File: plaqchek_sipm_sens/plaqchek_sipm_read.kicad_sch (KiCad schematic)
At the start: 32 parts, among them U2 OPA863A, U3 OPA863A, U4 OPA863A, U5 MCP1501T-50E, U9 MCP33131-10-E/MS

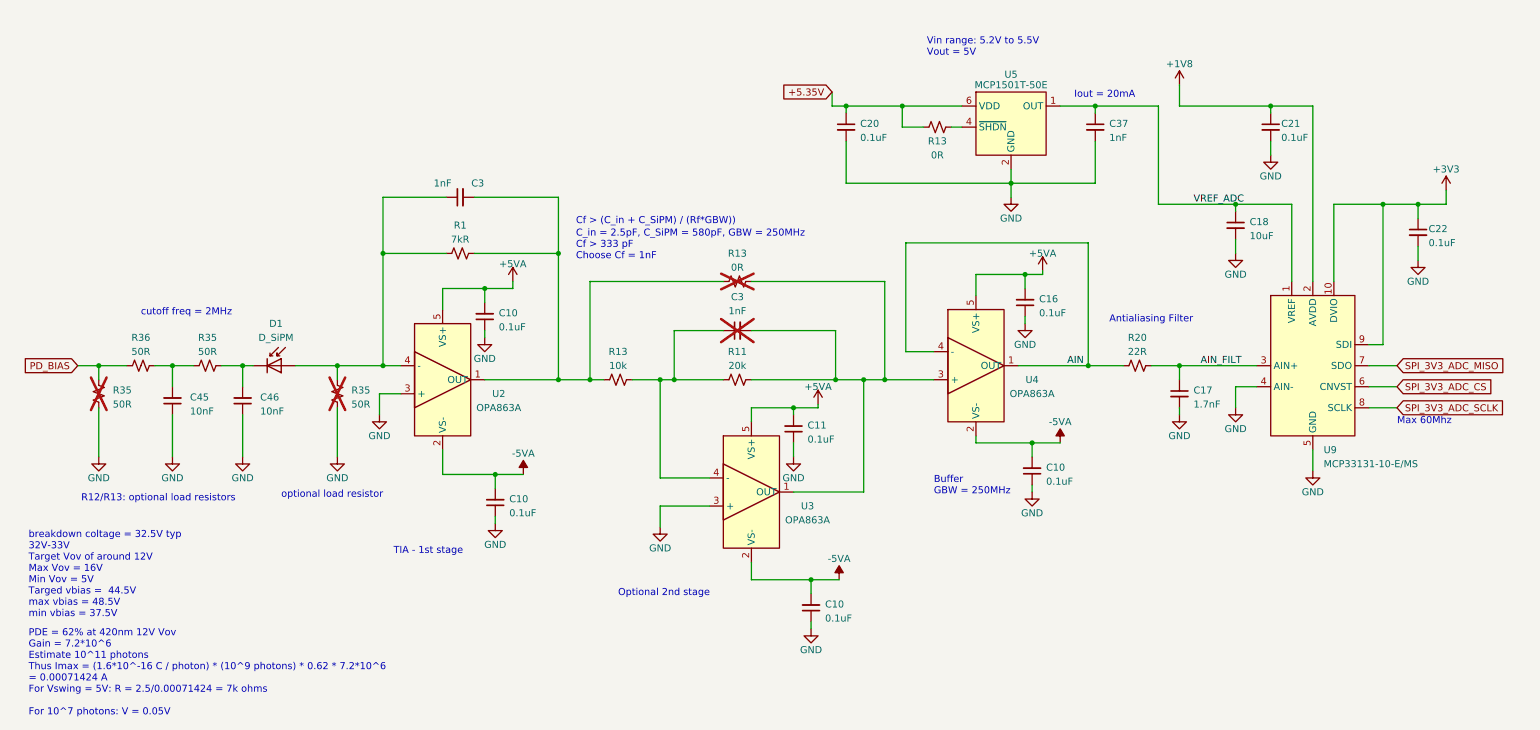
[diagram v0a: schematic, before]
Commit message: modify TIA feedback cap value for new op amp, assign some footprints
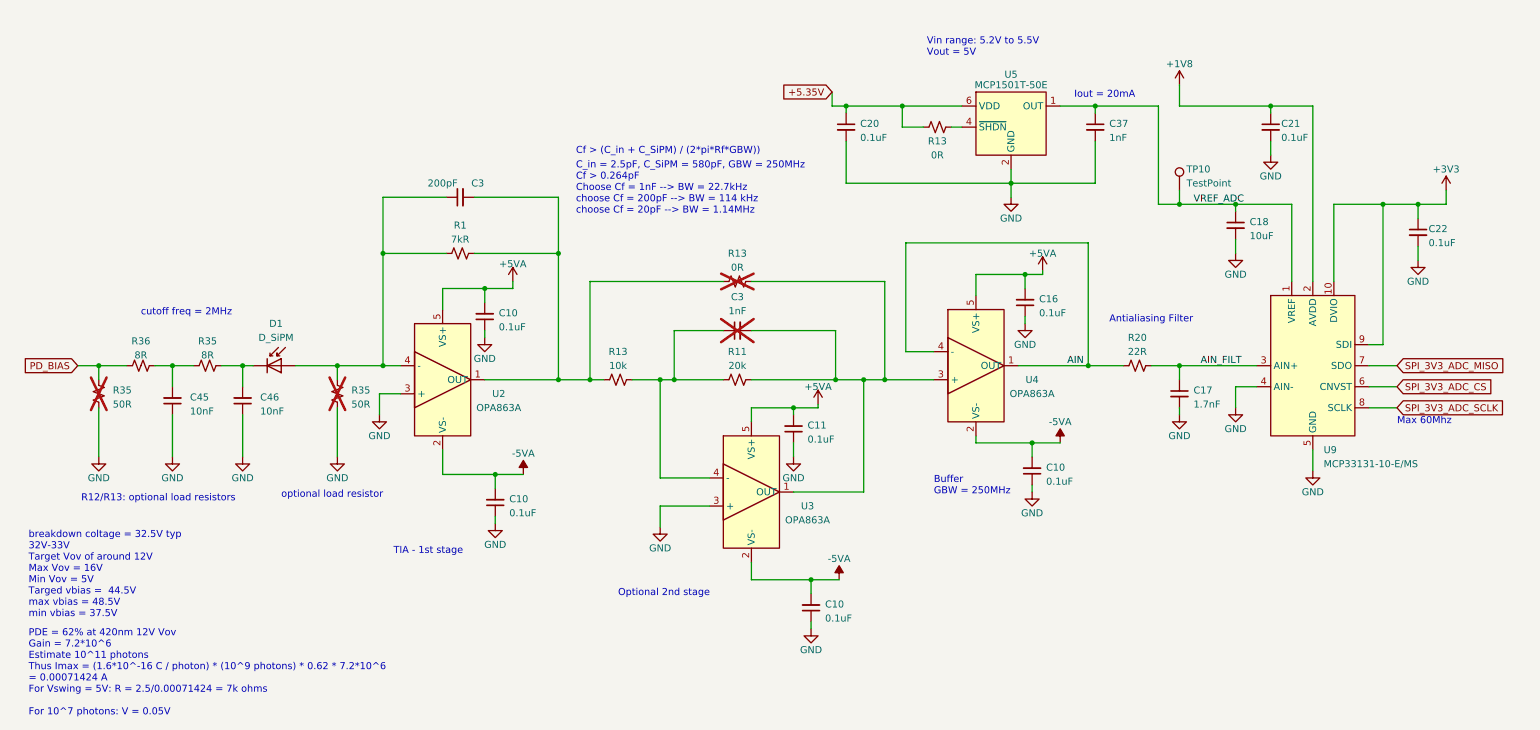
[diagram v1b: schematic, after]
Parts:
- added TP10: TestPoint, TestPoint:TestPoint_Pad_1.5x1.5mm, symbol Connector:TestPoint
- C10, C11, C16, C17, C18, C20, C21, C22, C3, C37, C45, C46: footprint (none) -> Capacitor_SMD:C_0603_1608Metric_Pad1.08x0.95mm_HandSolder
- C3: value 1nF -> 200pF; footprint (none) -> Capacitor_SMD:C_0603_1608Metric_Pad1.08x0.95mm_HandSolder
- R1, R11, R13, R20, R35: footprint (none) -> Resistor_SMD:R_0603_1608Metric_Pad0.98x0.95mm_HandSolder
- R35, R36: value 50R -> 8R; footprint (none) -> Resistor_SMD:R_0603_1608Metric_Pad0.98x0.95mm_HandSolder
- U5: footprint (none) -> Package_TO_SOT_SMD:SOT-23-6_Handsoldering
- U9: footprint (none) -> Package_DFN_QFN:WDFN-10-1EP_3x3mm_P0.5mm_EP1.8x2.5mm
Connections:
- net VREF_ADC: now also TP10.1
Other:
- note added: "C_in = 2.5pF, C_SiPM = 580pF, GBW = 250MHz Cf > 0.264pF Choose Cf = 1nF --> BW = 22.7kHz choose Cf = 200pF --> BW = 114 kHz choose Cf = 20pF --> BW = 1.14MHz"
- note added: "Cf > (C_in + C_SiPM) / (2*pi*Rf*GBW))"
- note removed: "C_in = 2.5pF, C_SiPM = 580pF, GBW = 250MHz Cf > 333 pF Choose Cf = 1nF"
- note removed: "Cf > (C_in + C_SiPM) / (Rf*GBW))"

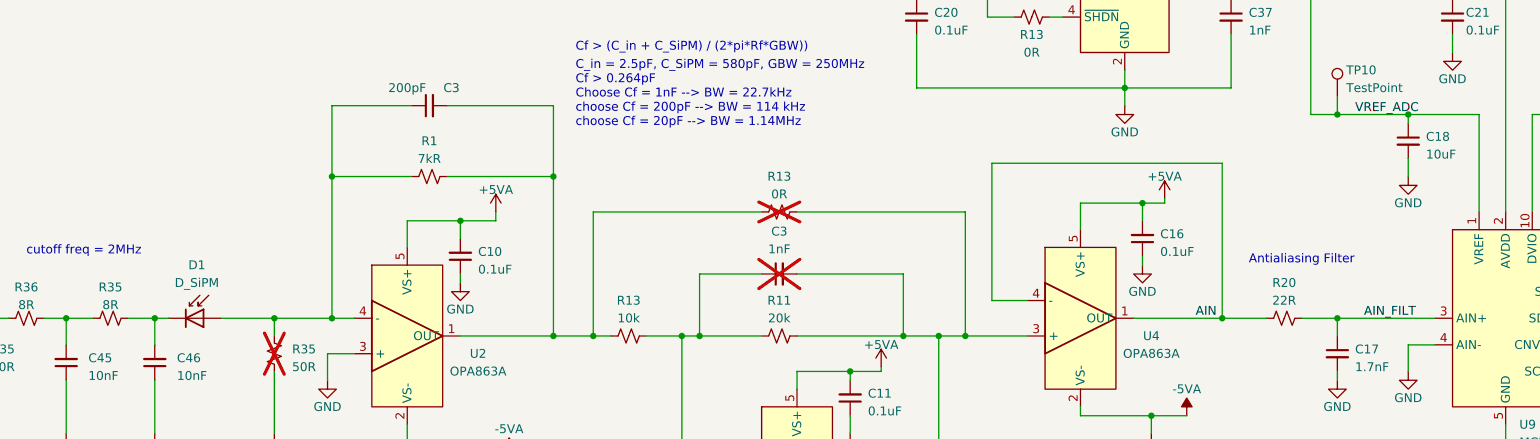
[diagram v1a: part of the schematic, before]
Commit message: more footprints and some value fixes
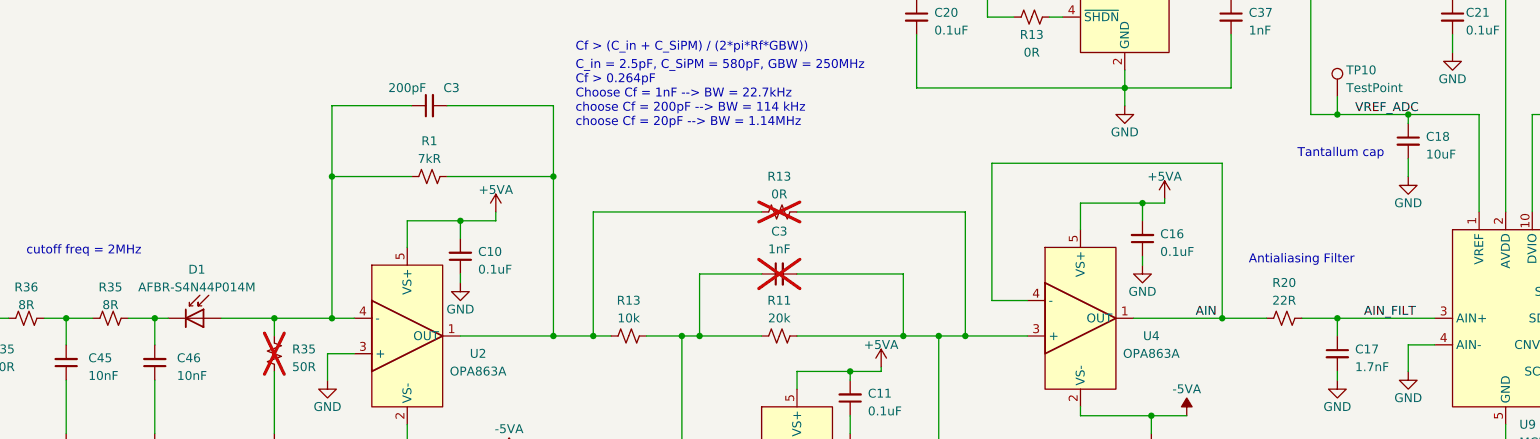
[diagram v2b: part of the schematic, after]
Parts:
- C18: footprint Capacitor_SMD:C_0603_1608Metric_Pad1.08x0.95mm_HandSolder -> Capacitor_SMD:C_0805_2012Metric_Pad1.18x1.45mm_HandSolder
- D1: value D_SiPM -> AFBR-S4N44P014M
- U9: footprint Package_DFN_QFN:WDFN-10-1EP_3x3mm_P0.5mm_EP1.8x2.5mm -> Package_SO:MSOP-10_3x3mm_P0.5mm
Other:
- note added: "Tantallum cap"
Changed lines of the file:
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@@
+    (effects (font (size 1.27 1.27)) (justify left bottom))
+  )
+  (text "Tantallum cap" (at 219.71 62.865 0)
     (effects (font (size 1.27 1.27)) (justify left bottom))
   )
@@
       (effects (font (size 1.27 1.27)) (justify left))
     )
-    (property "Footprint" "Capacitor_SMD:C_0603_1608Metric_Pad1.08x0.95mm_HandSolder" (at 235.585 60.325 0)
+    (property "Footprint" "Capacitor_SMD:C_0805_2012Metric_Pad1.18x1.45mm_HandSolder" (at 235.585 60.325 0)
       (effects (font (size 1.27 1.27)) hide)
     )
@@
       (effects (font (size 1.27 1.27)) (justify left))
     )
-    (property "Footprint" "Package_DFN_QFN:WDFN-10-1EP_3x3mm_P0.5mm_EP1.8x2.5mm" (at 249.555 80.645 0)
-      (effects (font (size 1.27 1.27)) hide)
-    )
-    (property "Datasheet" "" (at 249.555 80.645 0)
+    (property "Footprint" "Package_SO:MSOP-10_3x3mm_P0.5mm" (at 249.555 80.645 0)
+      (effects (font (size 1.27 1.27)) hide)
+    )
+    (property "Datasheet" "https://www.mouser.ca/datasheet/2/268/MCP33131_MCP33121_MCP33111_Family_Data_Sheet_DS200-3443670.pdf" (at 249.555 80.645 0)
       (effects (font (size 1.27 1.27)) hide)
     )
@@
   (symbol (lib_id "Device:D_SiPM") (at 61.595 85.725 0) (unit 1)
     (in_bom yes) (on_board yes) (dnp no) (fields_autoplaced)
-    (property "Reference" "D1" (at 61.9125 78.105 0)
-      (effects (font (size 1.27 1.27)))
-    )
-    (property "Value" "D_SiPM" (at 61.9125 80.645 0)
-      (effects (font (size 1.27 1.27)))
-    )
+    (property "Reference" "D1" (at 61.9125 78.74 0)
+      (effects (font (size 1.27 1.27)))
+    )
+    (property "Value" "AFBR-S4N44P014M" (at 61.9125 81.28 0)
+      (effects (font (size 1.27 1.27)))
+    )

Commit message: finish main logic board PCB routing
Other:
- note added: "14 bits Vref = 5V Resolution = 0.0003052V = 305.2µv"
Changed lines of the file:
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@@
+    (effects (font (size 1.27 1.27)) (justify left bottom))
+  )
+  (text "14 bits\nVref = 5V\nResolution = 0.0003052V = 305.2µv"
+    (at 238.76 27.94 0)
     (effects (font (size 1.27 1.27)) (justify left bottom))
   )

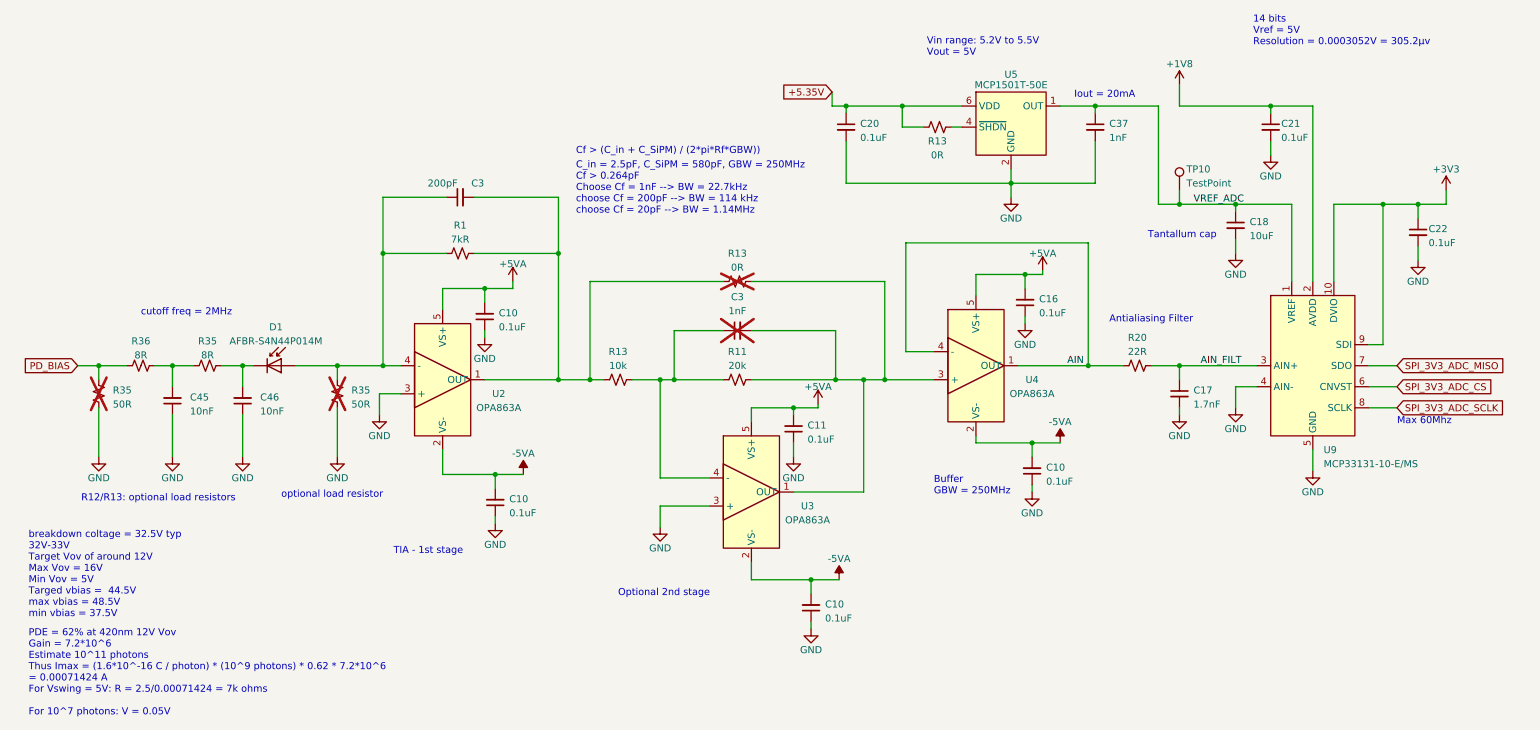
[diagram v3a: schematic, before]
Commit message: add sipm footprints, sensing board layout
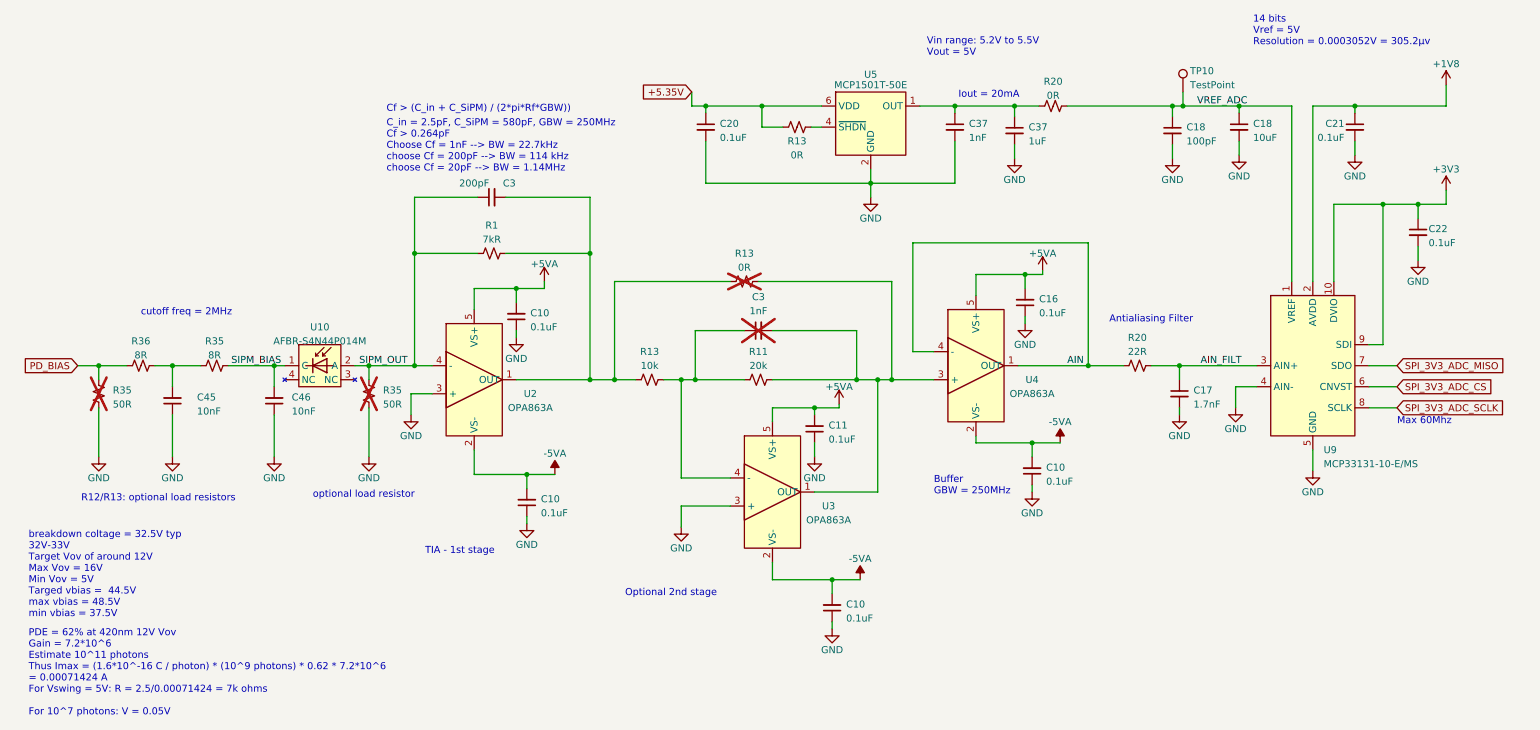
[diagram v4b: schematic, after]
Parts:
- removed D1: AFBR-S4N44P014M, symbol Device:D_SiPM
- added C18: 100pF, Capacitor_SMD:C_0603_1608Metric_Pad1.08x0.95mm_HandSolder, symbol Device:C_Small
- added C37: 1uF, Capacitor_SMD:C_0603_1608Metric_Pad1.08x0.95mm_HandSolder, symbol Device:C_Small
- added R20: 0R, Resistor_SMD:R_0603_1608Metric_Pad0.98x0.95mm_HandSolder, symbol Device:R_Small_US
- added U10: AFBR-S4N44P014M, plaqchek:AFBR-S4N44P014M-BREAKOUT, symbol plaqchek:AFBR-S4N44P014M-BREAKOUT
- TP10: footprint TestPoint:TestPoint_Pad_1.5x1.5mm -> TestPoint:TestPoint_Pad_D1.0mm
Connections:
- net GND: now also C18.2, C37.2
- net VREF_ADC: now also C18.1, R20.2; no longer C37.1, U5.1 (OUT)
- net SIPM_OUT: now reaches C3.1, R1.1, R35.2, U2.4 (-)
- net SIPM_OUT: now also U10.2 (A)
- net SIPM_BIAS: now reaches C46.2, R35.2
- net SIPM_BIAS: now also U10.1 (C)
- new net: C37.1, C37.1, R20.1, U5.1 (OUT)
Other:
- note removed: "Tantallum cap"
- moved on the sheet: C10, C11, C18, C20, C21, C3, C37, C46, R1, R11, R13, R35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

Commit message: start sensor board routing
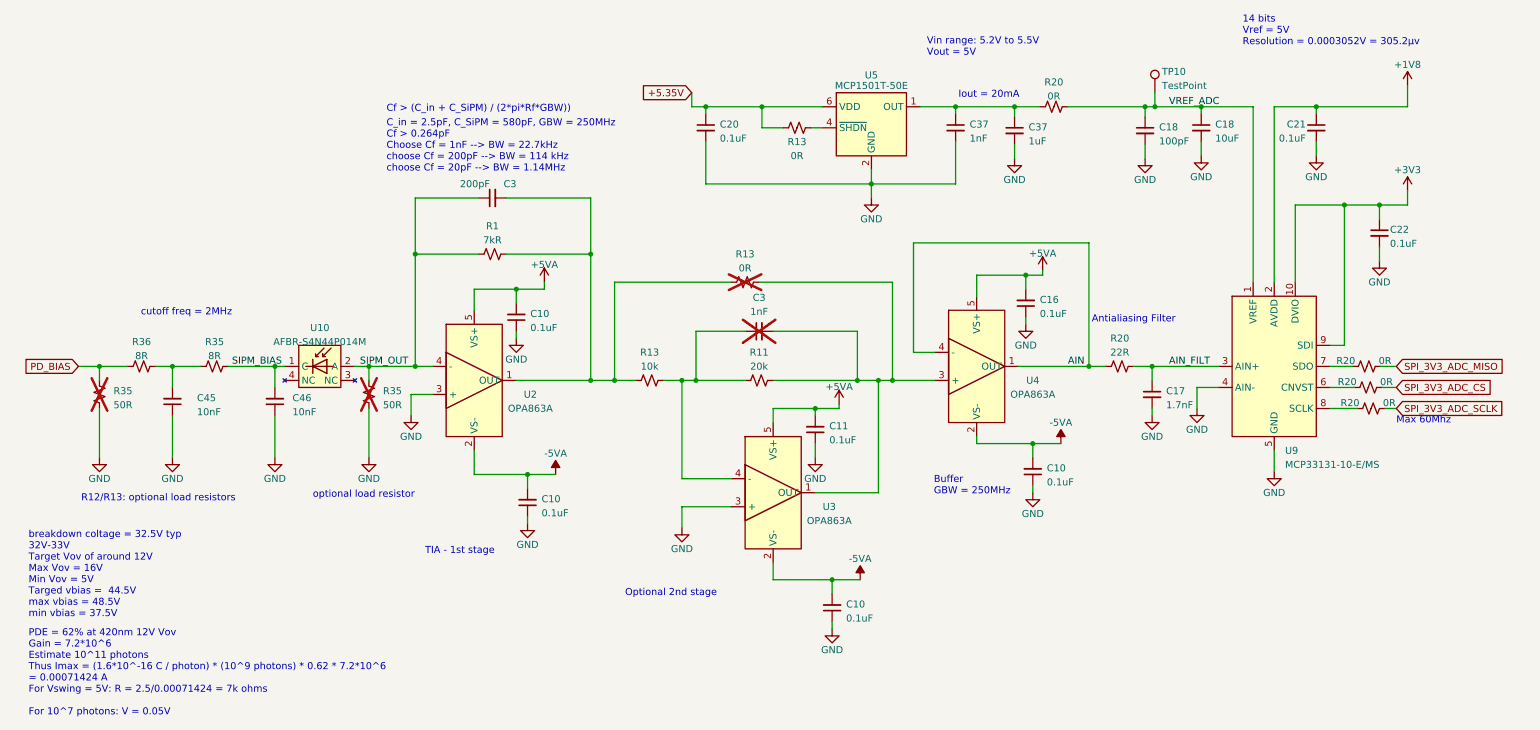
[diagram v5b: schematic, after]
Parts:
- added R20 (x3): 0R, Resistor_SMD:R_0603_1608Metric_Pad0.98x0.95mm_HandSolder, symbol Device:R_Small_US
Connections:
- net SPI_3V3_ADC_CS: now also R20.2; no longer U9.6 (CNVST)
- net SPI_3V3_ADC_MISO: now also R20.2; no longer U9.7 (SDO)
- net SPI_3V3_ADC_SCLK: now also R20.2; no longer U9.8 (SCLK)
- new net: R20.1, U9.8 (SCLK)
- new net: R20.1, U9.6 (CNVST)
- new net: R20.1, U9.7 (SDO)
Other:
- moved on the sheet: C17, C18, C21, C22, R20, TP10, U9

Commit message: finish routing sipm board
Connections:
- net +5.35V: now also R13.1; no longer R13.2
- net at U5.4 (~{SHDN}): now also R13.2; no longer R13.1
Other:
- moved on the sheet: C45, R13
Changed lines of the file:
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@@
     )
   )
-  (symbol (lib_id "Device:C_Small") (at 43.18 92.202 180) (unit 1)
-    (in_bom yes) (on_board yes) (dnp no)
-    (property "Reference" "C45" (at 47.625 91.5606 0)
+  (symbol (lib_id "Device:C_Small") (at 43.18 92.202 0) (mirror x) (unit 1)
+    (in_bom yes) (on_board yes) (dnp no)
+    (property "Reference" "C45" (at 38.735 91.5606 0)
       (effects (font (size 1.27 1.27)) (justify right))
     )
-    (property "Value" "10nF" (at 47.625 94.1006 0)
+    (property "Value" "10nF" (at 38.735 94.1006 0)
       (effects (font (size 1.27 1.27)) (justify right))
     )
@@
     )
   )
-  (symbol (lib_id "Device:R_Small_US") (at 156.21 42.672 270) (unit 1)
+  (symbol (lib_id "Device:R_Small_US") (at 156.21 42.672 90) (mirror x) (unit 1)
     (in_bom yes) (on_board yes) (dnp no)
     (property "Reference" "R13" (at 156.21 45.212 90)
